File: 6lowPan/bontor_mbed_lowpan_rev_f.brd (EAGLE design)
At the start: 98 x 107 mm, 170 parts, among them IC1 SIM900, IC2 74HC595D, IC3 74HC595D, IC4 ADE7758RW, IC5 74HC595D, J1 U.FL, U2 W5500, X1 NX2520SA

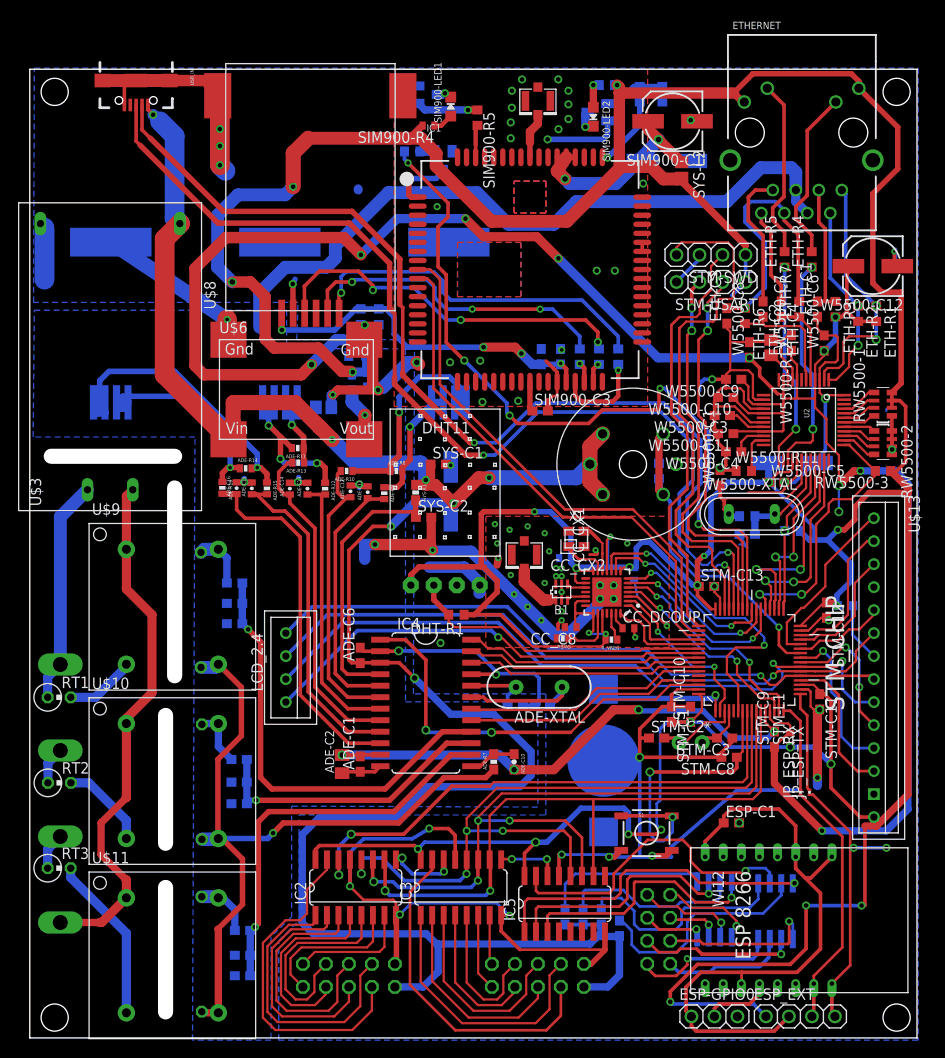
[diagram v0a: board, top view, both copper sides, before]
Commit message: update silkscreen and delete USB micro hole
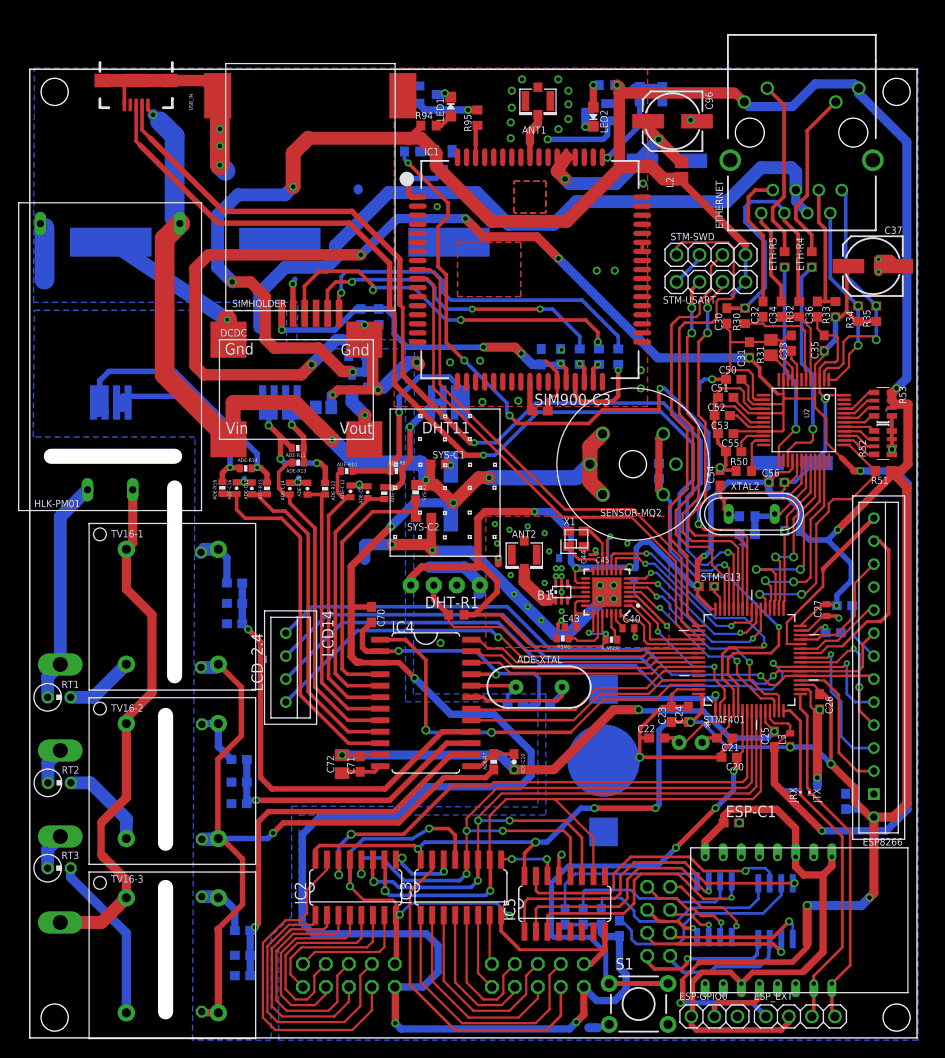
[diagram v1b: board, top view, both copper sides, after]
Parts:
- removed ADE-C6, STM-C10, STM-C12: 100nF, rcl:C0603
- removed SIM900-R4: 680R, rcl:R0402
- added C24, C70, LCD_C1: 100nF, rcl:C0603
- added C27: 100nF, rcl:C0402
- added C28: 4.7uF, rcl:C0603
- added R94: 680R, rcl:R0603
- ESP: value ESP8266WI12 -> ESP
- S1: device SparkFun-Electromechanical:TACTILE-SWITCH-SMD -> SparkFun-Electromechanical:TACTILE-PTH
- moved S1 18.9 mm to (67.2, 3.75)
- moved JP1 0.88 mm to (69.5, 12.9)
- renumbered ADE-C1 to C71, ADE-C2 to C72, ADE-C3 to C73, ADE-C4 to C74, CC_C14 to C46, CC_C20 to C41, CC_C8 to C43, CC_CX1 to C44, CC_CX2 to C45, CC_DCOUP to C40, ETH-C1 to C36, ETH-C2 to C32, ETH-C3 to C30, ETH-C4 to C34, ETH-R1 to R35, ETH-R2 to R34, ETH-R3 to R33, ETH-R6 to R30, ETH-R7 to R32, J1 to ANT2, JP_ESP_RX to JRX, JP_ESP_TX to JTX, PWR-SWT to PWR, RW5500-1 to R53, RW5500-2 to R52, RW5500-3 to R51, SIM900-C1 to C96, SIM900-C2 to C97, SIM900-LED1 to LED1, SIM900-LED2 to LED2, SIM900-R10 to R93, SIM900-R5 to R95, SIM900-R6 to R96, SIM900-R7 to R92, SIM900-R8 to R91, SIM900-R9 to R90, SIM900-T1 to T1, SIM900-T2 to T2, SIM900-T3 to T3, SIM_C1 to C80, SIM_C2 to C81, STM-C1 to C23, STM-C11 to C26, STM-C2 to C22, STM-C3 to C21, STM-C8 to C20, STM-C9 to C25, STM-L1 to L3, STM-XTAL to XTAL1, STM_CHIP to STMF401, SYS-C3 to C10, SYS-C4 to C11, SYS-L1 to L1, SYS-L2 to L2, SYS-R2 to R10, U$10 to TV16-2, U$11 to TV16-3, U$12 to TERM_BLOCK, U$13 to LCD14, U$14 to RJ-3, U$15 to RJ-2, U$16 to RJ-1, U$3 to HLK-PM01, U$5 to ESP, U$6 to DCDC, U$7 to ANT1, U$8 to SIMHOLDER, U$9 to TV16-1, W5500-C1 to C54, W5500-C10 to C51, W5500-C11 to C53, W5500-C12 to C37, W5500-C2 to C57, W5500-C3 to C52, W5500-C4 to C55, W5500-C5 to C56, W5500-C6 to C35, W5500-C7 to C33, W5500-C8 to C31, W5500-C9 to C50, W5500-R10 to R56, W5500-R11 to R50, W5500-R12 to R31, W5500-R13 to R54, W5500-XTAL to XTAL2
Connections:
- new net N$77: C28.1, STMF401.30
- net +5V: now also C70.1; no longer ADE-C6.1
- net CC_GPIO0: now also STMF401.5; no longer STMF401.6
- net DGND: now also C24.2, C27.2, C28.2, C70.2, LCD_C1.2; no longer ADE-C6.2, STM-C10.2, STM-C12.2
- net MQ2_DATA: now also STMF401.6; no longer STMF401.26
- net N$16: now also R94.1; no longer SIM900-R4.1
- net T_DO: now also STMF401.26; no longer STMF401.30
- net VDD: now also C24.1, C27.1, LCD_C1.1, R94.2; no longer SIM900-R4.2, STM-C10.1, STM-C12.1
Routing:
- net DGND: track 425.6 -> 386.4 mm, vias 73 -> 74
- net SWD_NRST: track 33.8 -> 56.3 mm, vias 2 -> 3
- net +5V: track 258.3 -> 271.4 mm, vias 7 -> 9
- net VDD: track 578.7 -> 568.2 mm, vias 25 -> 26
- net MQ2_DATA: track 35.8 -> 45.6 mm
- net VCC: track 249.7 -> 242.5 mm, vias 11 -> 9
- net T_DO: track 15.9 -> 20.6 mm
- net ESP_TX: track 31.6 -> 27.6 mm, vias 2 -> 0
- net N$77: track 0.00 -> 3.76 mm, vias 0 -> 1
- net CH1_IN: track 34.9 -> 32.3 mm
- net N$5: track 24.7 -> 22.7 mm
- net SR_RST: track 72.3 -> 74.1 mm
- net CH2_B: track 17.9 -> 16.2 mm
- net N$6: track 26.7 -> 25.2 mm
- net T: track 5.34 -> 4.08 mm
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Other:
- board text added: "ANT1"
- board text added: "ANT2"
- board text added: "ESP8266"
- board text added: "SENSOR-MQ2"
